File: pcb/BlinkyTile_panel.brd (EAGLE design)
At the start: 208.3 x 182.9 mm, 218 parts

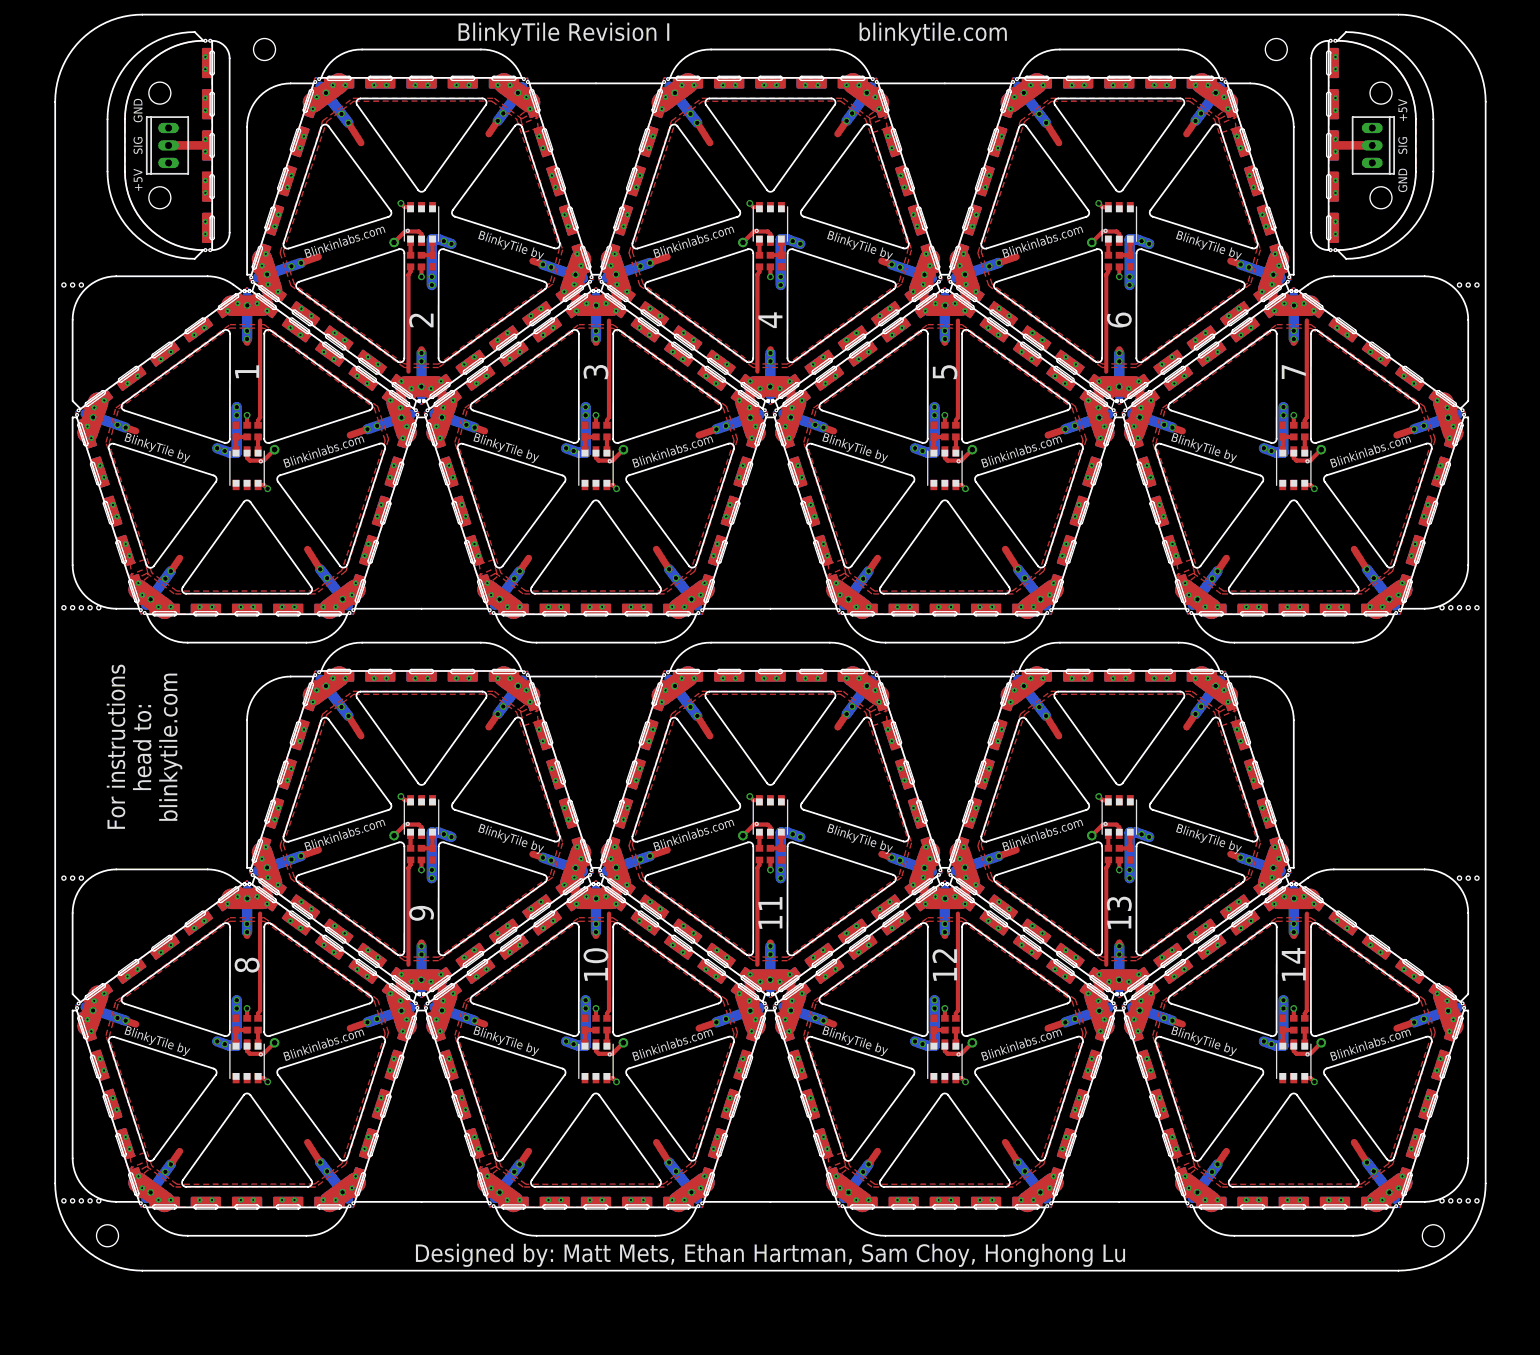
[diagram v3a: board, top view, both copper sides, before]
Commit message: Rev J panel: Add larger spaces in centers between tiles, tighten up edges.
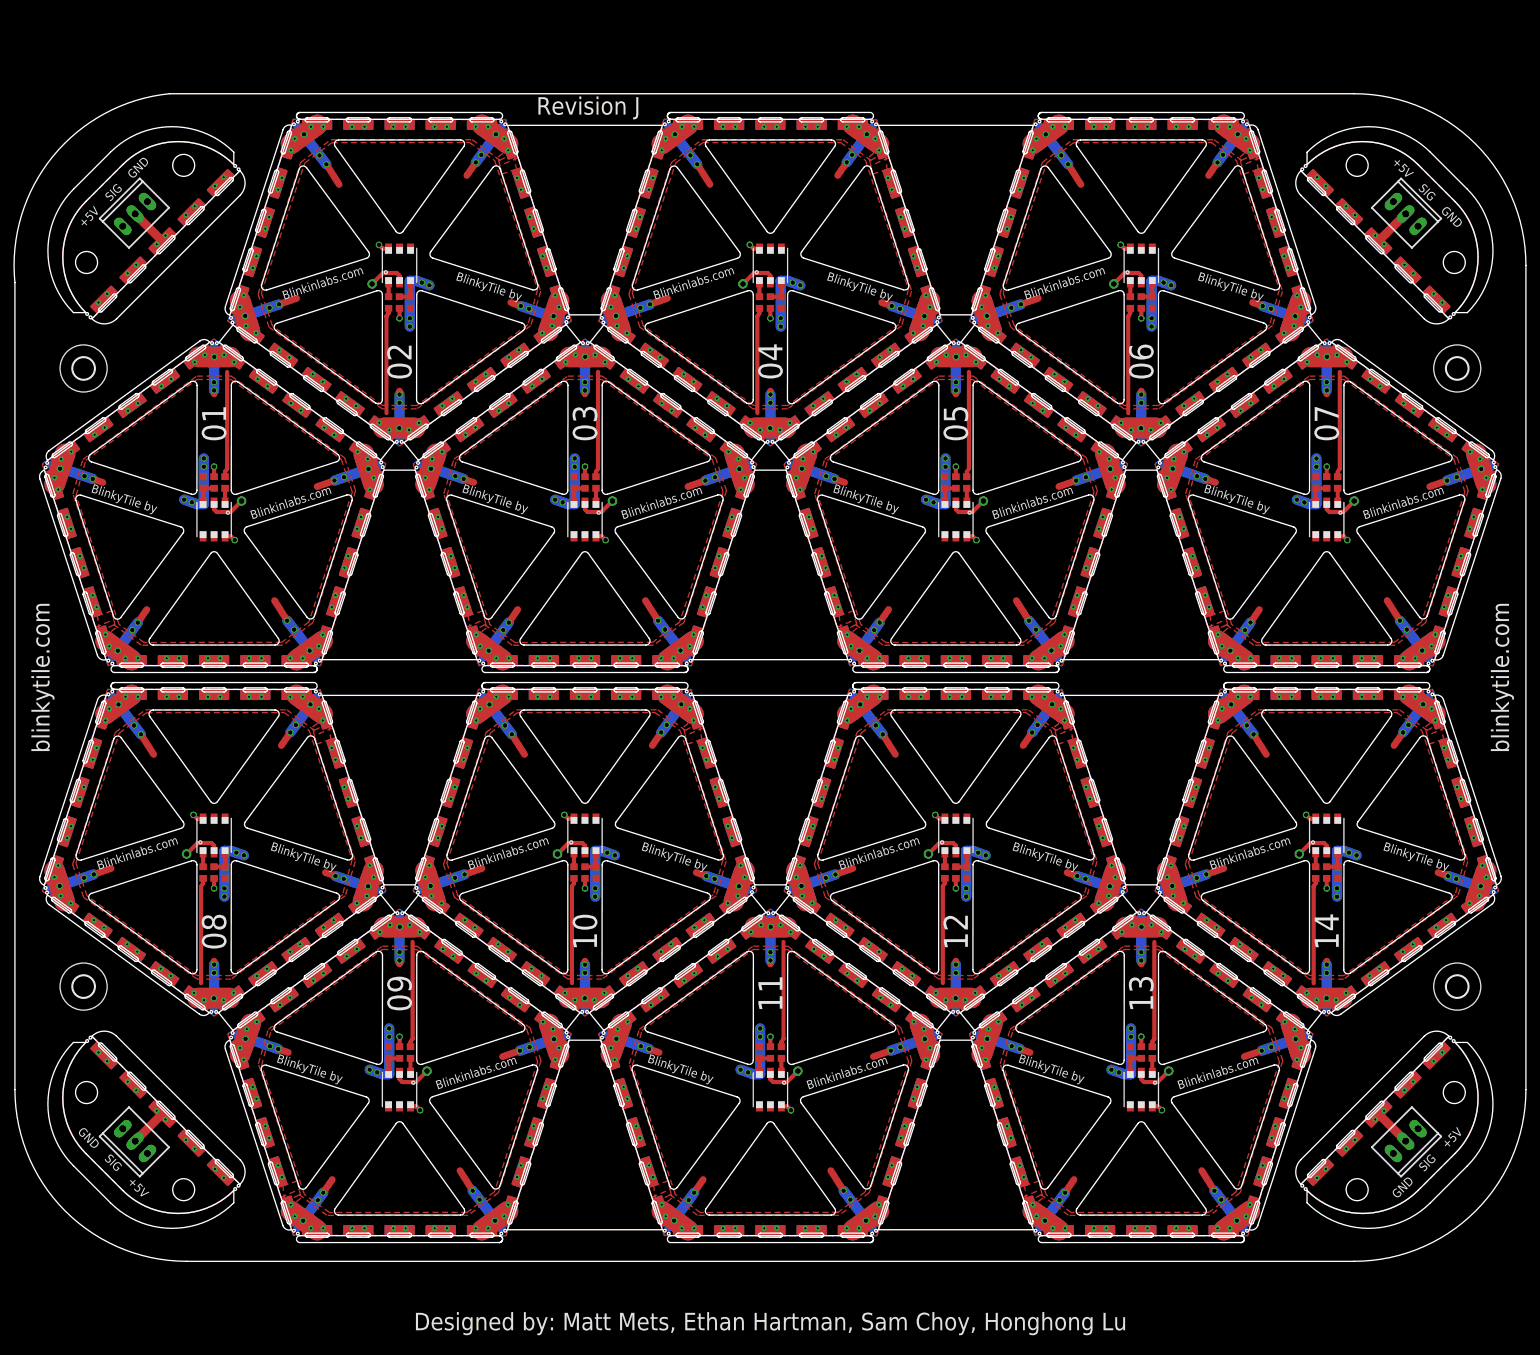
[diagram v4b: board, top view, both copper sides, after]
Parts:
- removed C4: .1uF, adafruit:C0603
- removed E$16, E$17, E$18, E$19, E$20, E$80, E$81, E$82: (no value), dodocohedreled:MOUSE_BITE_1
- removed R7: 75, adafruit:R0603
- removed R8: 10k, adafruit:R0603
- removed U$19, U$20, U$21, U$22, U$23: D_EDGEMOD, dodocohedreled:D_EDGE_SLOT_MOD
- removed U$24: WS2822S_LED, blinkinlabs:WS2822S_LED
- added C15: .1uF, adafruit:C0603
- added E$91, E$92, E$93, E$94: (no value), holes:3,2
- added R29: 75, adafruit:R0603
- added R30: 10k, adafruit:R0603
- added U$87, U$88, U$89, U$92, U$93, U$94, U$95: D_EDGEMOD, dodocohedreled:D_EDGE_SLOT_MOD
- added U$90: WS2822S_LED, blinkinlabs:WS2822S_LED
- E$49, E$52: device con-hdrs40:MTA-100-3V -> dodocohedreled:MOUSE_BITE_1
- E$76, E$79, E$85, E$88: device dodocohedreled:MOUSE_BITE_1 -> con-hdrs40:MTA-100-3V
- U$54, U$60, U$66, U$72, U$78, U$84: value D_EDGEMOD -> WS2822S_LED; device dodocohedreled:D_EDGE_SLOT_MOD -> blinkinlabs:WS2822S_LED
- U$56, U$62, U$68, U$74, U$80, U$86: value WS2822S_LED -> D_EDGEMOD; device blinkinlabs:WS2822S_LED -> dodocohedreled:D_EDGE_SLOT_MOD
- moved E$54 216.0 mm to (78.4, -52.0), turned to 288 degrees
- moved E$53 208.0 mm to (69.1, -80.8), turned to 216 degrees
- moved E$52 202.6 mm to (38.9, -80.7), turned to 144 degrees
- moved E$87 192.1 mm to (-99.2, -52.7), turned to 45 degrees
- moved U$86 181.7 mm to (-101.2, -16.5), turned to 252 degrees
- moved E$77 180.0 mm to (-99.2, 52.7), turned to 135 degrees
- moved E$85 172.8 mm to (-92.5, -67.5), turned to 135 degrees
- moved U$50 170.3 mm to (60.8, -16.5), turned to 252 degrees
- moved E$76 153.1 mm to (-92.5, 67.5), turned to 45 degrees
- moved U$81 150.8 mm to (-74.2, -66.5), turned to 288 degrees
- moved U$85 149.4 mm to (-81.0, -1.80), turned to 180 degrees
- moved E$78 145.1 mm to (-77.7, 74.2), turned to 315 degrees
- moved U$84 144.3 mm to (-54.0, -60.0), turned to 270 degrees
- moved U$53 140.8 mm to (93.4, -40.2), turned to 36 degrees
- moved U$51 140.3 mm to (101.2, -16.5), turned to 108 degrees
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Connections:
- removed net 5V3: R7.1, U$19.P$2, U$19.P$4, U$19.P$7, U$19.P$9, U$19.PWRVIA1, U$19.PWRVIA3, U$19.PWRVIA4, U$19.PWRVIA6, U$20.P$2, U$20.P$4, U$20.P$7, U$20.P$9, U$20.PWRVIA1, U$20.PWRVIA3, U$20.PWRVIA4, U$20.PWRVIA6, U$21.P$2, U$21.P$4, U$21.P$7, U$21.P$9, U$21.PWRVIA1, U$21.PWRVIA3, U$21.PWRVIA4, U$21.PWRVIA6, U$22.P$2, U$22.P$4, U$22.P$7, U$22.P$9, U$22.PWRVIA1, U$22.PWRVIA3, U$22.PWRVIA4, U$22.PWRVIA6, U$23.P$2, U$23.P$4, U$23.P$7, U$23.P$9, U$23.PWRVIA1, U$23.PWRVIA3, U$23.PWRVIA4, U$23.PWRVIA6, U$24.6
- removed net ADRI3: U$24.2
- removed net DATA3: R8.2, U$19.P$3, U$19.P$8, U$19.SIGVIA1, U$19.SIGVIA3, U$20.P$3, U$20.P$8, U$20.SIGVIA1, U$20.SIGVIA3, U$21.P$3, U$21.P$8, U$21.SIGVIA1, U$21.SIGVIA3, U$22.P$3, U$22.P$8, U$22.SIGVIA1, U$22.SIGVIA3, U$23.P$3, U$23.P$8, U$23.SIGVIA1, U$23.SIGVIA3
- removed net GND3: C4.2, U$19.GNDVIA1, U$19.GNDVIA3, U$19.GNDVIA4, U$19.GNDVIA6, U$19.P$1, U$19.P$10, U$19.P$5, U$19.P$6, U$20.GNDVIA1, U$20.GNDVIA3, U$20.GNDVIA4, U$20.GNDVIA6, U$20.P$1, U$20.P$10, U$20.P$5, U$20.P$6, U$21.GNDVIA1, U$21.GNDVIA3, U$21.GNDVIA4, U$21.GNDVIA6, U$21.P$1, U$21.P$10, U$21.P$5, U$21.P$6, U$22.GNDVIA1, U$22.GNDVIA3, U$22.GNDVIA4, U$22.GNDVIA6, U$22.P$1, U$22.P$10, U$22.P$5, U$22.P$6, U$23.GNDVIA1, U$23.GNDVIA3, U$23.GNDVIA4, U$23.GNDVIA6, U$23.P$1, U$23.P$10, U$23.P$5, U$23.P$6, U$24.4
- removed net N$11: C4.1, R7.2, U$24.3
- removed net N$12: R8.1, U$24.1
- removed net S$7: E$52.2, U$50.P$3
- removed net S$8: E$52.3, U$50.P$1, U$50.P$5
- removed net S$9: E$52.1, U$50.P$7, U$50.P$9
- new net 5V: R1.1, U$2.P$2, U$2.P$4, U$2.P$7, U$2.P$9, U$2.PWRVIA1, U$2.PWRVIA3, U$2.PWRVIA4, U$2.PWRVIA6, U$3.P$2, U$3.P$4, U$3.P$7, U$3.P$9, U$3.PWRVIA1, U$3.PWRVIA3, U$3.PWRVIA4, U$3.PWRVIA6, U$4.P$2, U$4.P$4, U$4.P$7, U$4.P$9, U$4.PWRVIA1, U$4.PWRVIA3, U$4.PWRVIA4, U$4.PWRVIA6, U$5.P$2, U$5.P$4, U$5.P$7, U$5.P$9, U$5.PWRVIA1, U$5.PWRVIA3, U$5.PWRVIA4, U$5.PWRVIA6, U$6.P$2, U$6.P$4, U$6.P$7, U$6.P$9, U$6.PWRVIA1, U$6.PWRVIA3, U$6.PWRVIA4, U$6.PWRVIA6, U$7.6
- new net ADRI: U$7.2
- new net DATA: R2.2, U$2.P$3, U$2.P$8, U$2.SIGVIA1, U$2.SIGVIA3, U$3.P$3, U$3.P$8, U$3.SIGVIA1, U$3.SIGVIA3, U$4.P$3, U$4.P$8, U$4.SIGVIA1, U$4.SIGVIA3, U$5.P$3, U$5.P$8, U$5.SIGVIA1, U$5.SIGVIA3, U$6.P$3, U$6.P$8, U$6.SIGVIA1, U$6.SIGVIA3
- new net GND: C1.2, U$2.GNDVIA1, U$2.GNDVIA3, U$2.GNDVIA4, U$2.GNDVIA6, U$2.P$1, U$2.P$10, U$2.P$5, U$2.P$6, U$3.GNDVIA1, U$3.GNDVIA3, U$3.GNDVIA4, U$3.GNDVIA6, U$3.P$1, U$3.P$10, U$3.P$5, U$3.P$6, U$4.GNDVIA1, U$4.GNDVIA3, U$4.GNDVIA4, U$4.GNDVIA6, U$4.P$1, U$4.P$10, U$4.P$5, U$4.P$6, U$5.GNDVIA1, U$5.GNDVIA3, U$5.GNDVIA4, U$5.GNDVIA6, U$5.P$1, U$5.P$10, U$5.P$5, U$5.P$6, U$6.GNDVIA1, U$6.GNDVIA3, U$6.GNDVIA4, U$6.GNDVIA6, U$6.P$1, U$6.P$10, U$6.P$5, U$6.P$6, U$7.4
- new net N$44: C15.1, R29.2, U$90.3
- new net N$45: R30.1, U$90.1
- new net S$1: E$76.2, U$92.P$3
- new net S$10: E$85.2, U$94.P$3
- new net S$11: E$85.3, U$94.P$1, U$94.P$5
- new net S$12: E$85.1, U$94.P$7, U$94.P$9
- new net S$13: E$88.2, U$95.P$3
- new net S$14: E$88.3, U$95.P$1, U$95.P$5
- new net S$15: E$88.1, U$95.P$7, U$95.P$9
- new net S$2: E$76.3, U$92.P$1, U$92.P$5
- new net S$3: E$76.1, U$92.P$7, U$92.P$9
- net 5V10: now also R21.1, U$62.P$2, U$62.P$4, U$62.P$7, U$62.P$9, U$62.PWRVIA1, U$62.PWRVIA3, U$62.PWRVIA4, U$62.PWRVIA6, U$63.P$2, U$63.P$4, U$63.P$7, U$63.P$9, U$63.PWRVIA1, U$63.PWRVIA3, U$63.PWRVIA4, U$63.PWRVIA6, U$64.P$2, U$64.P$4, U$64.P$7, U$64.P$9, U$64.PWRVIA1, U$64.PWRVIA3, U$64.PWRVIA4, U$64.PWRVIA6, U$65.P$2, U$65.P$4, U$65.P$7, U$65.P$9, U$65.PWRVIA1, U$65.PWRVIA3, U$65.PWRVIA4, U$65.PWRVIA6, U$66.6; no longer R19.1, U$57.P$2, U$57.P$4, U$57.P$7, U$57.P$9, U$57.PWRVIA1, U$57.PWRVIA3, U$57.PWRVIA4, U$57.PWRVIA6, U$58.P$2, U$58.P$4, U$58.P$7, U$58.P$9, U$58.PWRVIA1, U$58.PWRVIA3, U$58.PWRVIA4, U$58.PWRVIA6, U$59.P$2, U$59.P$4, U$59.P$7, U$59.P$9, U$59.PWRVIA1, U$59.PWRVIA3, U$59.PWRVIA4, U$59.PWRVIA6, U$60.P$2, U$60.P$4, U$60.P$7, U$60.P$9, U$60.PWRVIA1, U$60.PWRVIA3, U$60.PWRVIA4, U$60.PWRVIA6, U$62.6
- net 5V11: now also R23.1, U$68.P$2, U$68.P$4, U$68.P$7, U$68.P$9, U$68.PWRVIA1, U$68.PWRVIA3, U$68.PWRVIA4, U$68.PWRVIA6, U$69.P$2, U$69.P$4, U$69.P$7, U$69.P$9, U$69.PWRVIA1, U$69.PWRVIA3, U$69.PWRVIA4, U$69.PWRVIA6, U$70.P$2, U$70.P$4, U$70.P$7, U$70.P$9, U$70.PWRVIA1, U$70.PWRVIA3, U$70.PWRVIA4, U$70.PWRVIA6, U$71.P$2, U$71.P$4, U$71.P$7, U$71.P$9, U$71.PWRVIA1, U$71.PWRVIA3, U$71.PWRVIA4, U$71.PWRVIA6, U$72.6; no longer R21.1, U$63.P$2, U$63.P$4, U$63.P$7, U$63.P$9, U$63.PWRVIA1, U$63.PWRVIA3, U$63.PWRVIA4, U$63.PWRVIA6, U$64.P$2, U$64.P$4, U$64.P$7, U$64.P$9, U$64.PWRVIA1, U$64.PWRVIA3, U$64.PWRVIA4, U$64.PWRVIA6, U$65.P$2, U$65.P$4, U$65.P$7, U$65.P$9, U$65.PWRVIA1, U$65.PWRVIA3, U$65.PWRVIA4, U$65.PWRVIA6, U$66.P$2, U$66.P$4, U$66.P$7, U$66.P$9, U$66.PWRVIA1, U$66.PWRVIA3, U$66.PWRVIA4, U$66.PWRVIA6, U$68.6
- net 5V12: now also R25.1, U$74.P$2, U$74.P$4, U$74.P$7, U$74.P$9, U$74.PWRVIA1, U$74.PWRVIA3, U$74.PWRVIA4, U$74.PWRVIA6, U$75.P$2, U$75.P$4, U$75.P$7, U$75.P$9, U$75.PWRVIA1, U$75.PWRVIA3, U$75.PWRVIA4, U$75.PWRVIA6, U$76.P$2, U$76.P$4, U$76.P$7, U$76.P$9, U$76.PWRVIA1, U$76.PWRVIA3, U$76.PWRVIA4, U$76.PWRVIA6, U$77.P$2, U$77.P$4, U$77.P$7, U$77.P$9, U$77.PWRVIA1, U$77.PWRVIA3, U$77.PWRVIA4, U$77.PWRVIA6, U$78.6; no longer R23.1, U$69.P$2, U$69.P$4, U$69.P$7, U$69.P$9, U$69.PWRVIA1, U$69.PWRVIA3, U$69.PWRVIA4, U$69.PWRVIA6, U$70.P$2, U$70.P$4, U$70.P$7, U$70.P$9, U$70.PWRVIA1, U$70.PWRVIA3, U$70.PWRVIA4, U$70.PWRVIA6, U$71.P$2, U$71.P$4, U$71.P$7, U$71.P$9, U$71.PWRVIA1, U$71.PWRVIA3, U$71.PWRVIA4, U$71.PWRVIA6, U$72.P$2, U$72.P$4, U$72.P$7, U$72.P$9, U$72.PWRVIA1, U$72.PWRVIA3, U$72.PWRVIA4, U$72.PWRVIA6, U$74.6
- net 5V13: now also R27.1, U$80.P$2, U$80.P$4, U$80.P$7, U$80.P$9, U$80.PWRVIA1, U$80.PWRVIA3, U$80.PWRVIA4, U$80.PWRVIA6, U$81.P$2, U$81.P$4, U$81.P$7, U$81.P$9, U$81.PWRVIA1, U$81.PWRVIA3, U$81.PWRVIA4, U$81.PWRVIA6, U$82.P$2, U$82.P$4, U$82.P$7, U$82.P$9, U$82.PWRVIA1, U$82.PWRVIA3, U$82.PWRVIA4, U$82.PWRVIA6, U$83.P$2, U$83.P$4, U$83.P$7, U$83.P$9, U$83.PWRVIA1, U$83.PWRVIA3, U$83.PWRVIA4, U$83.PWRVIA6, U$84.6; no longer R25.1, U$75.P$2, U$75.P$4, U$75.P$7, U$75.P$9, U$75.PWRVIA1, U$75.PWRVIA3, U$75.PWRVIA4, U$75.PWRVIA6, U$76.P$2, U$76.P$4, U$76.P$7, U$76.P$9, U$76.PWRVIA1, U$76.PWRVIA3, U$76.PWRVIA4, U$76.PWRVIA6, U$77.P$2, U$77.P$4, U$77.P$7, U$77.P$9, U$77.PWRVIA1, U$77.PWRVIA3, U$77.PWRVIA4, U$77.PWRVIA6, U$78.P$2, U$78.P$4, U$78.P$7, U$78.P$9, U$78.PWRVIA1, U$78.PWRVIA3, U$78.PWRVIA4, U$78.PWRVIA6, U$80.6
- net 5V14: now also R29.1, U$86.P$2, U$86.P$4, U$86.P$7, U$86.P$9, U$86.PWRVIA1, U$86.PWRVIA3, U$86.PWRVIA4, U$86.PWRVIA6, U$87.P$2, U$87.P$4, U$87.P$7, U$87.P$9, U$87.PWRVIA1, U$87.PWRVIA3, U$87.PWRVIA4, U$87.PWRVIA6, U$88.P$2, U$88.P$4, U$88.P$7, U$88.P$9, U$88.PWRVIA1, U$88.PWRVIA3, U$88.PWRVIA4, U$88.PWRVIA6, U$89.P$2, U$89.P$4, U$89.P$7, U$89.P$9, U$89.PWRVIA1, U$89.PWRVIA3, U$89.PWRVIA4, U$89.PWRVIA6, U$90.6; no longer R27.1, U$81.P$2, U$81.P$4, U$81.P$7, U$81.P$9, U$81.PWRVIA1, U$81.PWRVIA3, U$81.PWRVIA4, U$81.PWRVIA6, U$82.P$2, U$82.P$4, U$82.P$7, U$82.P$9, U$82.PWRVIA1, U$82.PWRVIA3, U$82.PWRVIA4, U$82.PWRVIA6, U$83.P$2, U$83.P$4, U$83.P$7, U$83.P$9, U$83.PWRVIA1, U$83.PWRVIA3, U$83.PWRVIA4, U$83.PWRVIA6, U$84.P$2, U$84.P$4, U$84.P$7, U$84.P$9, U$84.PWRVIA1, U$84.PWRVIA3, U$84.PWRVIA4, U$84.PWRVIA6, U$86.6
- net 5V8: now also R17.1, U$49.P$2, U$49.P$4, U$49.P$7, U$49.P$9, U$49.PWRVIA1, U$49.PWRVIA3, U$49.PWRVIA4, U$49.PWRVIA6, U$50.P$2, U$50.P$4, U$50.P$7, U$50.P$9, U$50.PWRVIA1, U$50.PWRVIA3, U$50.PWRVIA4, U$50.PWRVIA6, U$51.P$2, U$51.P$4, U$51.P$7, U$51.P$9, U$51.PWRVIA1, U$51.PWRVIA3, U$51.PWRVIA4, U$51.PWRVIA6, U$52.P$2, U$52.P$4, U$52.P$7, U$52.P$9, U$52.PWRVIA1, U$52.PWRVIA3, U$52.PWRVIA4, U$52.PWRVIA6, U$53.P$2, U$53.P$4, U$53.P$7, U$53.P$9, U$53.PWRVIA1, U$53.PWRVIA3, U$53.PWRVIA4, U$53.PWRVIA6, U$54.6; no longer R1.1, U$2.P$2, U$2.P$4, U$2.P$7, U$2.P$9, U$2.PWRVIA1, U$2.PWRVIA3, U$2.PWRVIA4, U$2.PWRVIA6, U$3.P$2, U$3.P$4, U$3.P$7, U$3.P$9, U$3.PWRVIA1, U$3.PWRVIA3, U$3.PWRVIA4, U$3.PWRVIA6, U$4.P$2, U$4.P$4, U$4.P$7, U$4.P$9, U$4.PWRVIA1, U$4.PWRVIA3, U$4.PWRVIA4, U$4.PWRVIA6, U$5.P$2, U$5.P$4, U$5.P$7, U$5.P$9, U$5.PWRVIA1, U$5.PWRVIA3, U$5.PWRVIA4, U$5.PWRVIA6, U$6.P$2, U$6.P$4, U$6.P$7, U$6.P$9, U$6.PWRVIA1, U$6.PWRVIA3, U$6.PWRVIA4, U$6.PWRVIA6, U$7.6
- net 5V9: now also R19.1, U$56.P$2, U$56.P$4, U$56.P$7, U$56.P$9, U$56.PWRVIA1, U$56.PWRVIA3, U$56.PWRVIA4, U$56.PWRVIA6, U$57.P$2, U$57.P$4, U$57.P$7, U$57.P$9, U$57.PWRVIA1, U$57.PWRVIA3, U$57.PWRVIA4, U$57.PWRVIA6, U$58.P$2, U$58.P$4, U$58.P$7, U$58.P$9, U$58.PWRVIA1, U$58.PWRVIA3, U$58.PWRVIA4, U$58.PWRVIA6, U$59.P$2, U$59.P$4, U$59.P$7, U$59.P$9, U$59.PWRVIA1, U$59.PWRVIA3, U$59.PWRVIA4, U$59.PWRVIA6, U$60.6; no longer R17.1, U$51.P$2, U$51.P$4, U$51.P$7, U$51.P$9, U$51.PWRVIA1, U$51.PWRVIA3, U$51.PWRVIA4, U$51.PWRVIA6, U$52.P$2, U$52.P$4, U$52.P$7, U$52.P$9, U$52.PWRVIA1, U$52.PWRVIA3, U$52.PWRVIA4, U$52.PWRVIA6, U$53.P$2, U$53.P$4, U$53.P$7, U$53.P$9, U$53.PWRVIA1, U$53.PWRVIA3, U$53.PWRVIA4, U$53.PWRVIA6, U$54.P$2, U$54.P$4, U$54.P$7, U$54.P$9, U$54.PWRVIA1, U$54.PWRVIA3, U$54.PWRVIA4, U$54.PWRVIA6, U$56.6
- net ADRI10: now also U$66.2; no longer U$62.2
- net ADRI11: now also U$72.2; no longer U$68.2
- net ADRI12: now also U$78.2; no longer U$74.2
- net ADRI13: now also U$84.2; no longer U$80.2
- net ADRI14: now also U$90.2; no longer U$86.2
- net ADRI8: now also U$54.2; no longer U$7.2
- net ADRI9: now also U$60.2; no longer U$56.2
- net DATA10: now also R22.2, U$62.P$3, U$62.P$8, U$62.SIGVIA1, U$62.SIGVIA3, U$63.P$3, U$63.P$8, U$63.SIGVIA1, U$63.SIGVIA3, U$64.P$3, U$64.P$8, U$64.SIGVIA1, U$64.SIGVIA3, U$65.P$3, U$65.P$8, U$65.SIGVIA1, U$65.SIGVIA3; no longer R20.2, U$57.P$3, U$57.P$8, U$57.SIGVIA1, U$57.SIGVIA3, U$58.P$3, U$58.P$8, U$58.SIGVIA1, U$58.SIGVIA3, U$59.P$3, U$59.P$8, U$59.SIGVIA1, U$59.SIGVIA3, U$60.P$3, U$60.P$8, U$60.SIGVIA1, U$60.SIGVIA3
- net DATA11: now also R24.2, U$68.P$3, U$68.P$8, U$68.SIGVIA1, U$68.SIGVIA3, U$69.P$3, U$69.P$8, U$69.SIGVIA1, U$69.SIGVIA3, U$70.P$3, U$70.P$8, U$70.SIGVIA1, U$70.SIGVIA3, U$71.P$3, U$71.P$8, U$71.SIGVIA1, U$71.SIGVIA3; no longer R22.2, U$63.P$3, U$63.P$8, U$63.SIGVIA1, U$63.SIGVIA3, U$64.P$3, U$64.P$8, U$64.SIGVIA1, U$64.SIGVIA3, U$65.P$3, U$65.P$8, U$65.SIGVIA1, U$65.SIGVIA3, U$66.P$3, U$66.P$8, U$66.SIGVIA1, U$66.SIGVIA3
- net DATA12: now also R26.2, U$74.P$3, U$74.P$8, U$74.SIGVIA1, U$74.SIGVIA3, U$75.P$3, U$75.P$8, U$75.SIGVIA1, U$75.SIGVIA3, U$76.P$3, U$76.P$8, U$76.SIGVIA1, U$76.SIGVIA3, U$77.P$3, U$77.P$8, U$77.SIGVIA1, U$77.SIGVIA3; no longer R24.2, U$69.P$3, U$69.P$8, U$69.SIGVIA1, U$69.SIGVIA3, U$70.P$3, U$70.P$8, U$70.SIGVIA1, U$70.SIGVIA3, U$71.P$3, U$71.P$8, U$71.SIGVIA1, U$71.SIGVIA3, U$72.P$3, U$72.P$8, U$72.SIGVIA1, U$72.SIGVIA3
- net DATA13: now also R28.2, U$80.P$3, U$80.P$8, U$80.SIGVIA1, U$80.SIGVIA3, U$81.P$3, U$81.P$8, U$81.SIGVIA1, U$81.SIGVIA3, U$82.P$3, U$82.P$8, U$82.SIGVIA1, U$82.SIGVIA3, U$83.P$3, U$83.P$8, U$83.SIGVIA1, U$83.SIGVIA3; no longer R26.2, U$75.P$3, U$75.P$8, U$75.SIGVIA1, U$75.SIGVIA3, U$76.P$3, U$76.P$8, U$76.SIGVIA1, U$76.SIGVIA3, U$77.P$3, U$77.P$8, U$77.SIGVIA1, U$77.SIGVIA3, U$78.P$3, U$78.P$8, U$78.SIGVIA1, U$78.SIGVIA3
- net DATA14: now also R30.2, U$86.P$3, U$86.P$8, U$86.SIGVIA1, U$86.SIGVIA3, U$87.P$3, U$87.P$8, U$87.SIGVIA1, U$87.SIGVIA3, U$88.P$3, U$88.P$8, U$88.SIGVIA1, U$88.SIGVIA3, U$89.P$3, U$89.P$8, U$89.SIGVIA1, U$89.SIGVIA3; no longer R28.2, U$81.P$3, U$81.P$8, U$81.SIGVIA1, U$81.SIGVIA3, U$82.P$3, U$82.P$8, U$82.SIGVIA1, U$82.SIGVIA3, U$83.P$3, U$83.P$8, U$83.SIGVIA1, U$83.SIGVIA3, U$84.P$3, U$84.P$8, U$84.SIGVIA1, U$84.SIGVIA3
- net DATA8: now also R18.2, U$49.P$3, U$49.P$8, U$49.SIGVIA1, U$49.SIGVIA3, U$50.P$3, U$50.P$8, U$50.SIGVIA1, U$50.SIGVIA3, U$51.P$3, U$51.P$8, U$51.SIGVIA1, U$51.SIGVIA3, U$52.P$3, U$52.P$8, U$52.SIGVIA1, U$52.SIGVIA3, U$53.P$3, U$53.P$8, U$53.SIGVIA1, U$53.SIGVIA3; no longer R2.2, U$2.P$3, U$2.P$8, U$2.SIGVIA1, U$2.SIGVIA3, U$3.P$3, U$3.P$8, U$3.SIGVIA1, U$3.SIGVIA3, U$4.P$3, U$4.P$8, U$4.SIGVIA1, U$4.SIGVIA3, U$5.P$3, U$5.P$8, U$5.SIGVIA1, U$5.SIGVIA3, U$6.P$3, U$6.P$8, U$6.SIGVIA1, U$6.SIGVIA3
- net DATA9: now also R20.2, U$56.P$3, U$56.P$8, U$56.SIGVIA1, U$56.SIGVIA3, U$57.P$3, U$57.P$8, U$57.SIGVIA1, U$57.SIGVIA3, U$58.P$3, U$58.P$8, U$58.SIGVIA1, U$58.SIGVIA3, U$59.P$3, U$59.P$8, U$59.SIGVIA1, U$59.SIGVIA3; no longer R18.2, U$51.P$3, U$51.P$8, U$51.SIGVIA1, U$51.SIGVIA3, U$52.P$3, U$52.P$8, U$52.SIGVIA1, U$52.SIGVIA3, U$53.P$3, U$53.P$8, U$53.SIGVIA1, U$53.SIGVIA3, U$54.P$3, U$54.P$8, U$54.SIGVIA1, U$54.SIGVIA3
- net GND10: now also C11.2, U$62.GNDVIA1, U$62.GNDVIA3, U$62.GNDVIA4, U$62.GNDVIA6, U$62.P$1, U$62.P$10, U$62.P$5, U$62.P$6, U$63.GNDVIA1, U$63.GNDVIA3, U$63.GNDVIA4, U$63.GNDVIA6, U$63.P$1, U$63.P$10, U$63.P$5, U$63.P$6, U$64.GNDVIA1, U$64.GNDVIA3, U$64.GNDVIA4, U$64.GNDVIA6, U$64.P$1, U$64.P$10, U$64.P$5, U$64.P$6, U$65.GNDVIA1, U$65.GNDVIA3, U$65.GNDVIA4, U$65.GNDVIA6, U$65.P$1, U$65.P$10, U$65.P$5, U$65.P$6, U$66.4; no longer C10.2, U$57.GNDVIA1, U$57.GNDVIA3, U$57.GNDVIA4, U$57.GNDVIA6, U$57.P$1, U$57.P$10, U$57.P$5, U$57.P$6, U$58.GNDVIA1, U$58.GNDVIA3, U$58.GNDVIA4, U$58.GNDVIA6, U$58.P$1, U$58.P$10, U$58.P$5, U$58.P$6, U$59.GNDVIA1, U$59.GNDVIA3, U$59.GNDVIA4, U$59.GNDVIA6, U$59.P$1, U$59.P$10, U$59.P$5, U$59.P$6, U$60.GNDVIA1, U$60.GNDVIA3, U$60.GNDVIA4, U$60.GNDVIA6, U$60.P$1, U$60.P$10, U$60.P$5, U$60.P$6, U$62.4
- net GND11: now also C12.2, U$68.GNDVIA1, U$68.GNDVIA3, U$68.GNDVIA4, U$68.GNDVIA6, U$68.P$1, U$68.P$10, U$68.P$5, U$68.P$6, U$69.GNDVIA1, U$69.GNDVIA3, U$69.GNDVIA4, U$69.GNDVIA6, U$69.P$1, U$69.P$10, U$69.P$5, U$69.P$6, U$70.GNDVIA1, U$70.GNDVIA3, U$70.GNDVIA4, U$70.GNDVIA6, U$70.P$1, U$70.P$10, U$70.P$5, U$70.P$6, U$71.GNDVIA1, U$71.GNDVIA3, U$71.GNDVIA4, U$71.GNDVIA6, U$71.P$1, U$71.P$10, U$71.P$5, U$71.P$6, U$72.4; no longer C11.2, U$63.GNDVIA1, U$63.GNDVIA3, U$63.GNDVIA4, U$63.GNDVIA6, U$63.P$1, U$63.P$10, U$63.P$5, U$63.P$6, U$64.GNDVIA1, U$64.GNDVIA3, U$64.GNDVIA4, U$64.GNDVIA6, U$64.P$1, U$64.P$10, U$64.P$5, U$64.P$6, U$65.GNDVIA1, U$65.GNDVIA3, U$65.GNDVIA4, U$65.GNDVIA6, U$65.P$1, U$65.P$10, U$65.P$5, U$65.P$6, U$66.GNDVIA1, U$66.GNDVIA3, U$66.GNDVIA4, U$66.GNDVIA6, U$66.P$1, U$66.P$10, U$66.P$5, U$66.P$6, U$68.4
- net GND12: now also C13.2, U$74.GNDVIA1, U$74.GNDVIA3, U$74.GNDVIA4, U$74.GNDVIA6, U$74.P$1, U$74.P$10, U$74.P$5, U$74.P$6, U$75.GNDVIA1, U$75.GNDVIA3, U$75.GNDVIA4, U$75.GNDVIA6, U$75.P$1, U$75.P$10, U$75.P$5, U$75.P$6, U$76.GNDVIA1, U$76.GNDVIA3, U$76.GNDVIA4, U$76.GNDVIA6, U$76.P$1, U$76.P$10, U$76.P$5, U$76.P$6, U$77.GNDVIA1, U$77.GNDVIA3, U$77.GNDVIA4, U$77.GNDVIA6, U$77.P$1, U$77.P$10, U$77.P$5, U$77.P$6, U$78.4; no longer C12.2, U$69.GNDVIA1, U$69.GNDVIA3, U$69.GNDVIA4, U$69.GNDVIA6, U$69.P$1, U$69.P$10, U$69.P$5, U$69.P$6, U$70.GNDVIA1, U$70.GNDVIA3, U$70.GNDVIA4, U$70.GNDVIA6, U$70.P$1, U$70.P$10, U$70.P$5, U$70.P$6, U$71.GNDVIA1, U$71.GNDVIA3, U$71.GNDVIA4, U$71.GNDVIA6, U$71.P$1, U$71.P$10, U$71.P$5, U$71.P$6, U$72.GNDVIA1, U$72.GNDVIA3, U$72.GNDVIA4, U$72.GNDVIA6, U$72.P$1, U$72.P$10, U$72.P$5, U$72.P$6, U$74.4
- net GND13: now also C14.2, U$80.GNDVIA1, U$80.GNDVIA3, U$80.GNDVIA4, U$80.GNDVIA6, U$80.P$1, U$80.P$10, U$80.P$5, U$80.P$6, U$81.GNDVIA1, U$81.GNDVIA3, U$81.GNDVIA4, U$81.GNDVIA6, U$81.P$1, U$81.P$10, U$81.P$5, U$81.P$6, U$82.GNDVIA1, U$82.GNDVIA3, U$82.GNDVIA4, U$82.GNDVIA6, U$82.P$1, U$82.P$10, U$82.P$5, U$82.P$6, U$83.GNDVIA1, U$83.GNDVIA3, U$83.GNDVIA4, U$83.GNDVIA6, U$83.P$1, U$83.P$10, U$83.P$5, U$83.P$6, U$84.4; no longer C13.2, U$75.GNDVIA1, U$75.GNDVIA3, U$75.GNDVIA4, U$75.GNDVIA6, U$75.P$1, U$75.P$10, U$75.P$5, U$75.P$6, U$76.GNDVIA1, U$76.GNDVIA3, U$76.GNDVIA4, U$76.GNDVIA6, U$76.P$1, U$76.P$10, U$76.P$5, U$76.P$6, U$77.GNDVIA1, U$77.GNDVIA3, U$77.GNDVIA4, U$77.GNDVIA6, U$77.P$1, U$77.P$10, U$77.P$5, U$77.P$6, U$78.GNDVIA1, U$78.GNDVIA3, U$78.GNDVIA4, U$78.GNDVIA6, U$78.P$1, U$78.P$10, U$78.P$5, U$78.P$6, U$80.4
- net GND14: now also C15.2, U$86.GNDVIA1, U$86.GNDVIA3, U$86.GNDVIA4, U$86.GNDVIA6, U$86.P$1, U$86.P$10, U$86.P$5, U$86.P$6, U$87.GNDVIA1, U$87.GNDVIA3, U$87.GNDVIA4, U$87.GNDVIA6, U$87.P$1, U$87.P$10, U$87.P$5, U$87.P$6, U$88.GNDVIA1, U$88.GNDVIA3, U$88.GNDVIA4, U$88.GNDVIA6, U$88.P$1, U$88.P$10, U$88.P$5, U$88.P$6, U$89.GNDVIA1, U$89.GNDVIA3, U$89.GNDVIA4, U$89.GNDVIA6, U$89.P$1, U$89.P$10, U$89.P$5, U$89.P$6, U$90.4; no longer C14.2, U$81.GNDVIA1, U$81.GNDVIA3, U$81.GNDVIA4, U$81.GNDVIA6, U$81.P$1, U$81.P$10, U$81.P$5, U$81.P$6, U$82.GNDVIA1, U$82.GNDVIA3, U$82.GNDVIA4, U$82.GNDVIA6, U$82.P$1, U$82.P$10, U$82.P$5, U$82.P$6, U$83.GNDVIA1, U$83.GNDVIA3, U$83.GNDVIA4, U$83.GNDVIA6, U$83.P$1, U$83.P$10, U$83.P$5, U$83.P$6, U$84.GNDVIA1, U$84.GNDVIA3, U$84.GNDVIA4, U$84.GNDVIA6, U$84.P$1, U$84.P$10, U$84.P$5, U$84.P$6, U$86.4
- net GND8: now also C9.2, U$49.GNDVIA1, U$49.GNDVIA3, U$49.GNDVIA4, U$49.GNDVIA6, U$49.P$1, U$49.P$10, U$49.P$5, U$49.P$6, U$50.GNDVIA1, U$50.GNDVIA3, U$50.GNDVIA4, U$50.GNDVIA6, U$50.P$1, U$50.P$10, U$50.P$5, U$50.P$6, U$51.GNDVIA1, U$51.GNDVIA3, U$51.GNDVIA4, U$51.GNDVIA6, U$51.P$1, U$51.P$10, U$51.P$5, U$51.P$6, U$52.GNDVIA1, U$52.GNDVIA3, U$52.GNDVIA4, U$52.GNDVIA6, U$52.P$1, U$52.P$10, U$52.P$5, U$52.P$6, U$53.GNDVIA1, U$53.GNDVIA3, U$53.GNDVIA4, U$53.GNDVIA6, U$53.P$1, U$53.P$10, U$53.P$5, U$53.P$6, U$54.4; no longer C1.2, U$2.GNDVIA1, U$2.GNDVIA3, U$2.GNDVIA4, U$2.GNDVIA6, U$2.P$1, U$2.P$10, U$2.P$5, U$2.P$6, U$3.GNDVIA1, U$3.GNDVIA3, U$3.GNDVIA4, U$3.GNDVIA6, U$3.P$1, U$3.P$10, U$3.P$5, U$3.P$6, U$4.GNDVIA1, U$4.GNDVIA3, U$4.GNDVIA4, U$4.GNDVIA6, U$4.P$1, U$4.P$10, U$4.P$5, U$4.P$6, U$5.GNDVIA1, U$5.GNDVIA3, U$5.GNDVIA4, U$5.GNDVIA6, U$5.P$1, U$5.P$10, U$5.P$5, U$5.P$6, U$6.GNDVIA1, U$6.GNDVIA3, U$6.GNDVIA4, U$6.GNDVIA6, U$6.P$1, U$6.P$10, U$6.P$5, U$6.P$6, U$7.4
- net GND9: now also C10.2, U$56.GNDVIA1, U$56.GNDVIA3, U$56.GNDVIA4, U$56.GNDVIA6, U$56.P$1, U$56.P$10, U$56.P$5, U$56.P$6, U$57.GNDVIA1, U$57.GNDVIA3, U$57.GNDVIA4, U$57.GNDVIA6, U$57.P$1, U$57.P$10, U$57.P$5, U$57.P$6, U$58.GNDVIA1, U$58.GNDVIA3, U$58.GNDVIA4, U$58.GNDVIA6, U$58.P$1, U$58.P$10, U$58.P$5, U$58.P$6, U$59.GNDVIA1, U$59.GNDVIA3, U$59.GNDVIA4, U$59.GNDVIA6, U$59.P$1, U$59.P$10, U$59.P$5, U$59.P$6, U$60.4; no longer C9.2, U$51.GNDVIA1, U$51.GNDVIA3, U$51.GNDVIA4, U$51.GNDVIA6, U$51.P$1, U$51.P$10, U$51.P$5, U$51.P$6, U$52.GNDVIA1, U$52.GNDVIA3, U$52.GNDVIA4, U$52.GNDVIA6, U$52.P$1, U$52.P$10, U$52.P$5, U$52.P$6, U$53.GNDVIA1, U$53.GNDVIA3, U$53.GNDVIA4, U$53.GNDVIA6, U$53.P$1, U$53.P$10, U$53.P$5, U$53.P$6, U$54.GNDVIA1, U$54.GNDVIA3, U$54.GNDVIA4, U$54.GNDVIA6, U$54.P$1, U$54.P$10, U$54.P$5, U$54.P$6, U$56.4
- net N$26: now also U$54.3; no longer U$56.3
- net N$27: now also U$54.1; no longer U$56.1
- net N$29: now also U$60.3; no longer U$62.3
- net N$30: now also U$60.1; no longer U$62.1
- net N$32: now also U$66.3; no longer U$68.3
- net N$33: now also U$66.1; no longer U$68.1
- net N$35: now also U$72.3; no longer U$74.3
- net N$36: now also U$72.1; no longer U$74.1
- net N$38: now also U$78.3; no longer U$80.3
- net N$39: now also U$78.1; no longer U$80.1
- net N$41: now also U$84.3; no longer U$86.3
- net N$42: now also U$84.1; no longer U$86.1
- net S$4: now also E$79.2, U$93.P$3; no longer E$49.2, U$49.P$3
- net S$5: now also E$79.3, U$93.P$1, U$93.P$5; no longer E$49.3, U$49.P$1, U$49.P$5
- net S$6: now also E$79.1, U$93.P$7, U$93.P$9; no longer E$49.1, U$49.P$7, U$49.P$9
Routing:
- net GND3: track 111.7 -> 0.00 mm, vias 19 -> 0
- net GND: track 0.00 -> 111.7 mm, vias 0 -> 19
- net DATA: track 0.00 -> 15.3 mm
- net DATA3: track 15.3 -> 0.00 mm
- net ADRI: track 0.00 -> 5.78 mm, vias 0 -> 1
- net ADRI3: track 5.78 -> 0.00 mm, vias 1 -> 0
- net S$10: track 0.00 -> 5.62 mm
- net S$7: track 5.62 -> 0.00 mm
- net S$1: track 0.00 -> 5.62 mm
- net S$13: track 0.00 -> 5.62 mm
- net N$44: track 0.00 -> 3.70 mm
- net N$11: track 3.70 -> 0.00 mm
- net 5V: track 0.00 -> 3.08 mm, vias 0 -> 2
- net 5V3: track 3.08 -> 0.00 mm, vias 2 -> 0
- net N$45: track 0.00 -> 2.10 mm
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- added copper zone on layer 16, net 5V
- added copper zone on layer 1, net DATA
- added copper zone on layer 1, net GND
- added copper zone on layer 1, net N$4
- added copper zone on layer 1, net N$43
- added copper zone on layer 1, net S$11
- added copper zone on layer 16, net S$12
- added copper zone on layer 1, net S$14
- added copper zone on layer 16, net S$15
- added copper zone on layer 1, net S$2
- added copper zone on layer 16, net S$3
- removed copper zone on layer 16, net 5V3
- removed copper zone on layer 1, net DATA3
- removed copper zone on layer 1, net GND3
- removed copper zone on layer 1, net N$1 (its old number)
- removed copper zone on layer 1, net N$10
- removed copper zone on layer 1, net S$8
- removed copper zone on layer 16, net S$9
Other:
- board size 208.3 x 182.9 mm -> 220.1 x 170 mm
- board text added: "01"
- board text added: "02"
- board text added: "03"
- board text added: "04"
- board text added: "05"
- board text added: "06"
- board text added: "07"
- board text added: "08"
- board text added: "09"
- board text added: "Revision J"
- board text removed: "1"
- board text removed: "2"
- board text removed: "3"
- board text removed: "4"
- board text removed: "5"
- board text removed: "6"
- board text removed: "7"
- board text removed: "8"
- board text removed: "9"
- board text removed: "BlinkyTile Revision I"
- board text removed: "For instructions head to: blinkytile.com"
